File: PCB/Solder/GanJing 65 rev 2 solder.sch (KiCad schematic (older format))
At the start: 150 parts, among them SW1 EC11_rotary_encoder, U1 Elite-C

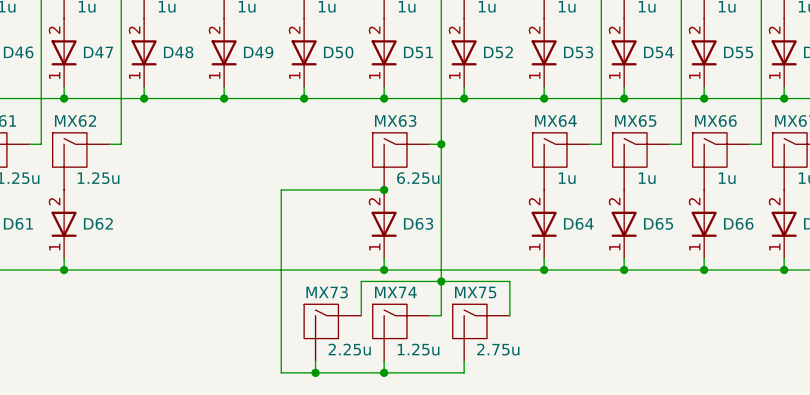
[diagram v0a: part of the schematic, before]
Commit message: Adding split spacebar to hotswap PCB
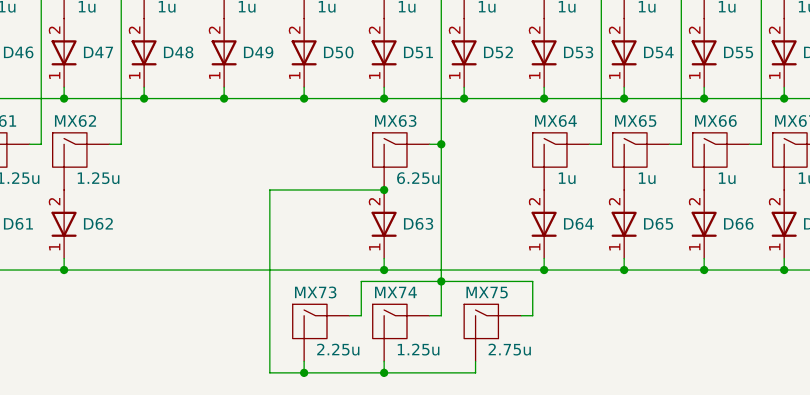
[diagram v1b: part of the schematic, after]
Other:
- moved on the sheet: MX73, MX75
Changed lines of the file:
@@
 	7700 5600 7700 5450
-Wire Wire Line
-	7700 5450 8000 5450
-Wire Wire Line
-	8000 5450 8000 5600
 Wire Wire Line
 	7350 5450 7350 5600
 Connection ~ 7700 5450
 Wire Wire Line
-	7150 5800 7150 5850
-Wire Wire Line
-	7150 5850 7450 5850
-Wire Wire Line
-	7800 5850 7800 5800
-Wire Wire Line
 	7450 5800 7450 5850
 Connection ~ 7450 5850
 Wire Wire Line
-	7450 5850 7800 5850
-Wire Wire Line
-	7450 5050 7000 5050
-Wire Wire Line
-	7000 5050 7000 5850
-Wire Wire Line
-	7000 5850 7150 5850
+	6950 5050 6950 5850
 Connection ~ 7450 5050
-Connection ~ 7150 5850
 Wire Wire Line
 	5950 1850 5950 2600
@@
 L GanJing_components:MX_2.25u_no_LED_flipped_stabs MX73
 U 1 1 61A6CF50
-P 7150 5600
-F 0 "MX73" H 7200 5700 50  0000 C CNN
-F 1 "MX_2.25u_no_LED_flipped_stabs" H 7150 5600 50  0001 C CNN
-F 2 "GanJing_components:MX_2.25u_no_LED_flipped_stabs" H 7150 5600 50  0001 C CNN
-F 3 "https://datasheet.octopart.com/MX1A-11NW-Cherry-datasheet-34676.pdf" H 7150 5600 50  0001 C CNN
-F 4 "2.25u" H 7300 5450 50  0000 C CNN "Size"
-	1    7150 5600
+P 7100 5600
+F 0 "MX73" H 7150 5700 50  0000 C CNN
+F 1 "MX_2.25u_no_LED_flipped_stabs" H 7100 5600 50  0001 C CNN
+F 2 "GanJing_components:MX_2.25u_no_LED_flipped_stabs" H 7100 5600 50  0001 C CNN
+F 3 "https://datasheet.octopart.com/MX1A-11NW-Cherry-datasheet-34676.pdf" H 7100 5600 50  0001 C CNN
+F 4 "2.25u" H 7250 5450 50  0000 C CNN "Size"
+	1    7100 5600
 	1    0    0    -1
 $EndComp
@@
 L GanJing_components:MX_2.75u_no_LED_flipped_stabs MX75
 U 1 1 61A6D9EF
-P 7800 5600
-F 0 "MX75" H 7850 5700 50  0000 C CNN
-F 1 "MX_2.75u_no_LED_flipped_stabs" H 7800 5600 50  0001 C CNN
-F 2 "GanJing_components:MX_2.75u_no_LED_flipped_stabs" H 7800 5600 50  0001 C CNN
-F 3 "https://datasheet.octopart.com/MX1A-11NW-Cherry-datasheet-34676.pdf" H 7800 5600 50  0001 C CNN
-F 4 "2.75u" H 7950 5450 50  0000 C CNN "Size"
-	1    7800 5600
+P 7850 5600
+F 0 "MX75" H 7900 5700 50  0000 C CNN
+F 1 "MX_2.75u_no_LED_flipped_stabs" H 7850 5600 50  0001 C CNN
+F 2 "GanJing_components:MX_2.75u_no_LED_flipped_stabs" H 7850 5600 50  0001 C CNN
+F 3 "https://datasheet.octopart.com/MX1A-11NW-Cherry-datasheet-34676.pdf" H 7850 5600 50  0001 C CNN
+F 4 "2.75u" H 8000 5450 50  0000 C CNN "Size"
+	1    7850 5600
 	1    0    0    -1
 $EndComp
@@
 Wire Wire Line
 	2050 3150 2050 3100
+Wire Wire Line
+	6950 5050 7450 5050
+Wire Wire Line
+	6950 5850 7100 5850
+Wire Wire Line
+	7100 5800 7100 5850
+Connection ~ 7100 5850
+Wire Wire Line
+	7100 5850 7450 5850
+Wire Wire Line
+	7850 5850 7850 5800
+Wire Wire Line
+	7450 5850 7850 5850
+Wire Wire Line
+	8050 5600 8100 5600
+Wire Wire Line
+	8100 5600 8100 5450
+Wire Wire Line
+	7700 5450 8100 5450
+Wire Wire Line
+	7350 5600 7300 5600
 $EndSCHEMATC

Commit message: finished firmware
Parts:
- removed D58: 1N4148TR_diode, GanJing_components:1N4148TR_diode, symbol GanJing_components:1N4148TR_diode
- renumbered D59 to D58, D60 to D59, D61 to D60, D62 to D61, D63 to D62, D64 to D63, D65 to D64, D66 to D65, D67 to D66, D68 to D67, D69 to D68, D70 to D69, D71 to D70, MX59 to MX58, MX60 to MX59, MX61 to MX60, MX62 to MX61, MX63 to MX62, MX64 to MX63, MX65 to MX64, MX66 to MX65, MX67 to MX66, MX68 to MX67, MX69 to MX68, MX70 to MX69, MX71 to MX70, MX72 to MX71, MX73 to MX72, MX74 to MX73, MX75 to MX74, MX58 to MX75
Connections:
- net at D43.2, MX43.2 (ROW): now also MX75.2 (ROW)
